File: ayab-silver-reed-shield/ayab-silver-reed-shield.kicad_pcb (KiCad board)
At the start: 2 copper layers, 68.6 x 53.3 mm, 19 parts, among them J1 Power, J2 Digital/PWM, J3 Analog, J4 Digital/PWM, J5 DIN-7, J6 Barrel_Jack, K1 Relay_SPST-NO, Q1 2N2222A-TO92

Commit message: Update PCB design
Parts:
- removed C2: 100u, Locals:CP_6.3x11mm_horiz-R
- added C1: 100u, Locals:CP_6.3x11mm_horiz-R, F.Cu at (125.8, 89.0)
- D1: footprint Diode_THT:D_T-1_P5.08mm_Horizontal -> Diode_THT:D_DO-41_SOD81_P7.62mm_Horizontal
- Q1: footprint PCM_Package_TO_SOT_THT_AKL:TO-92_Inline_Wide_EBC -> Package_TO_SOT_THT:TO-92_Inline
- moved D1 1.76 mm to (115.0, 61.8)
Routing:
- net Net-(D1-A): track 27.2 -> 33.0 mm
- net Net-(C1-Pad1): track 22.3 -> 24.0 mm
- net Net-(Q1-B): track 7.32 -> 7.85 mm

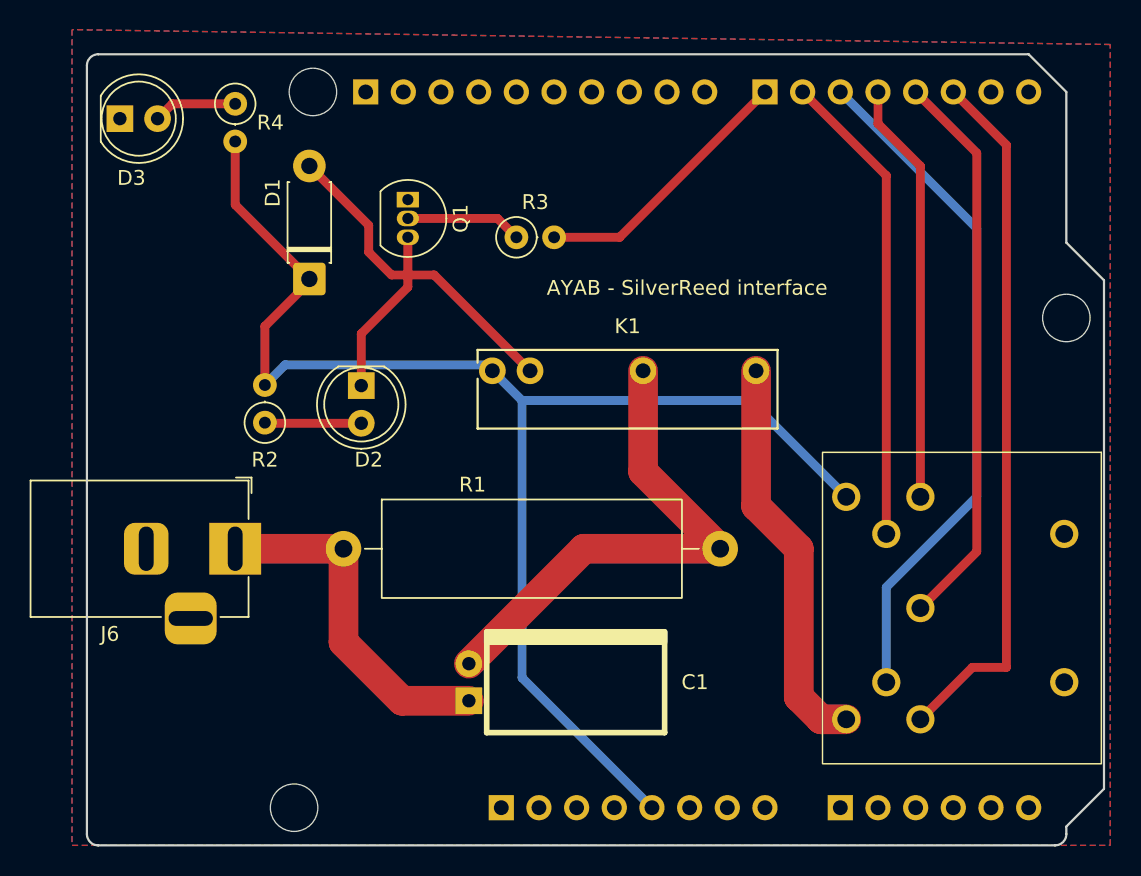
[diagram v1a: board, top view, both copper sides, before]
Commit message: fix: invert din pins
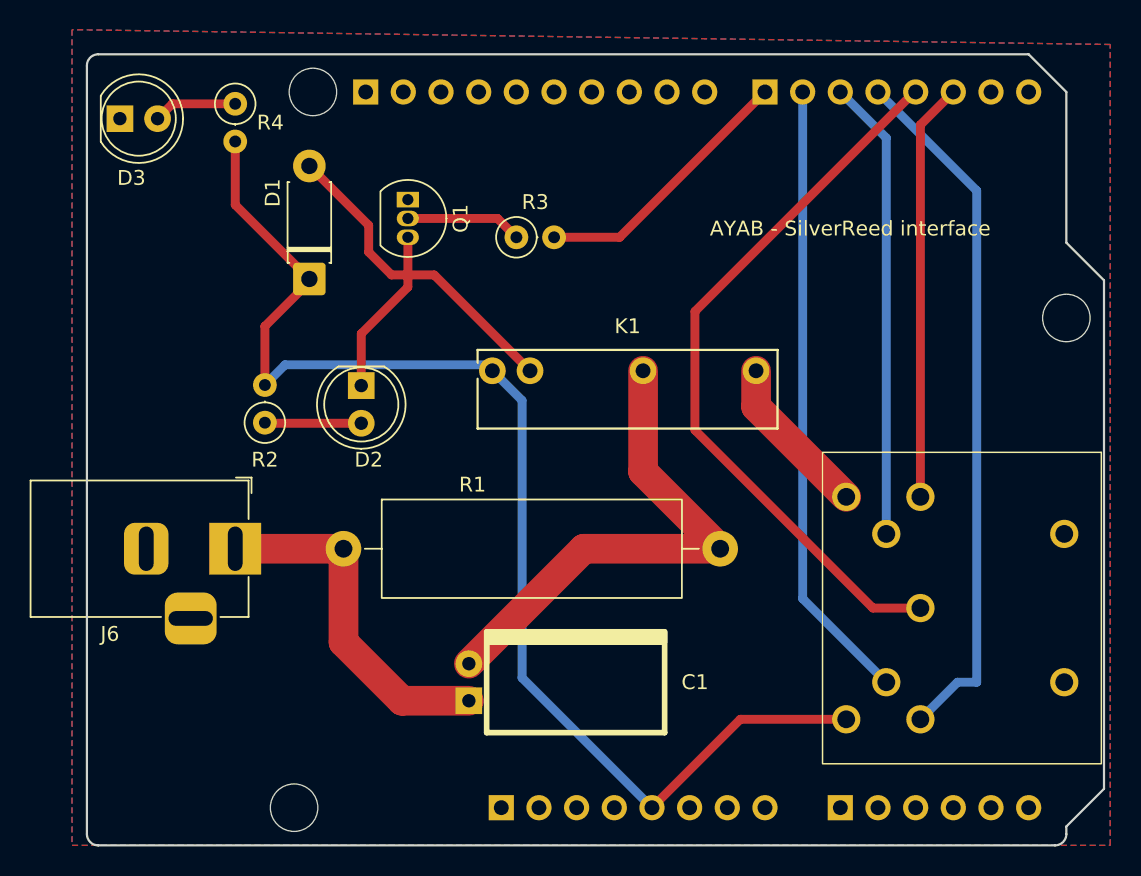
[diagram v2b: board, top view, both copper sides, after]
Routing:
- net /2: track 47.5 -> 28.2 mm
- net /4: track 28.6 -> 47.5 mm
- net Net-(J5-Pad6): track 27.0 -> 11.0 mm
- net /*5: track 46.1 -> 31.1 mm
- net /*3: track 38.1 -> 49.2 mm
- net /*6: track 32.1 -> 42.1 mm
- net +5V: track 94.3 -> 85.3 mm
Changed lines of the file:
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@@
 		(grid_origin 100 100)
 		(pcbplotparams
-			(layerselection 0x00000000_00000000_55555555_5555fff5)
+			(layerselection 0x00000000_00000000_55555555_5755f5ff)
 			(plot_on_all_layers_selection 0x00000000_00000000_00000000_00000000)
 			(disableapertmacros no)
 			(usegerberextensions no)
-			(usegerberattributes yes)
-			(usegerberadvancedattributes yes)
-			(creategerberjobfile yes)
+			(usegerberattributes no)
+			(usegerberadvancedattributes no)
+			(creategerberjobfile no)
 			(dashed_line_dash_ratio 12.000000)
 			(dashed_line_gap_ratio 3.000000)
@@
 			(drillshape 0)
 			(scaleselection 1)
-			(outputdirectory "../../../Downloads/")
+			(outputdirectory "Gerber/")
 		)
 	)
@@
 		)
 		(pad "1" thru_hole circle
-			(at 7.5 2.8 270)
+			(at -7.5 2.8 270)
 			(size 1.905 1.905)
 			(drill 1.2)
@@
 		)
 		(pad "3" thru_hole circle
-			(at -7.5 2.8 270)
+			(at 7.5 2.8 270)
 			(size 1.905 1.905)
 			(drill 1.2)
@@
 		)
 		(pad "4" thru_hole circle
-			(at 5 5.1 270)
+			(at -5 5.1 270)
 			(size 1.905 1.905)
 			(drill 1.2)
@@
 		)
 		(pad "5" thru_hole circle
-			(at -5 5.1 270)
+			(at 5 5.1 270)
 			(size 1.905 1.905)
 			(drill 1.2)
@@
 		)
 		(pad "6" thru_hole circle
-			(at 7.5 7.8 270)
+			(at -7.5 7.8 270)
 			(size 1.905 1.905)
 			(drill 1.2)
@@
 		)
 		(pad "7" thru_hole circle
-			(at -7.5 7.8 270)
+			(at 7.5 7.8 270)
 			(size 1.905 1.905)
 			(drill 1.2)
@@
 			(remove_unused_layers no)
 			(net 1 "GND")
-			(pinfunction "GNG")
+			(pinfunction "GND")
 			(pintype "passive")
 		)
@@
 			(remove_unused_layers no)
 			(net 1 "GND")
-			(pinfunction "GNG")
+			(pinfunction "GND")
 			(pintype "passive")
 		)
@@
 	)
 	(gr_text "AYAB - SilverReed interface\n"
-		(at 131 63 0)
+		(at 142 59 0)
 		(layer "F.SilkS")
 		(effects
@@
 	)
 	(segment
+		(start 138.1 97.46)
+		(end 144.06 91.5)
+		(width 0.6)
+		(layer "F.Cu")
+		(net 3)
+	)
+	(segment
 		(start 110 56.81)
 		(end 115 61.81)
@@
 	)
 	(segment
-		(start 144.7 70)
-		(end 129.34 70)
+		(start 144.06 91.5)
+		(end 151.2 91.5)
 		(width 0.6)
-		(layer "B.Cu")
+		(layer "F.Cu")
 		(net 3)
 	)
@@
 	)
 	(segment
-		(start 151.2 76.5)
-		(end 144.7 70)
-		(width 0.6)
-		(layer "B.Cu")
-		(net 3)
-	)
-	(segment
 		(start 135.92 59)
 		(end 145.72 49.2)
@@
 	(segment
 		(start 153.34 49.2)
-		(end 153.34 51.34)
+		(end 153.2 49.2)
 		(width 0.6)
 		(layer "F.Cu")
@@
 	)
 	(segment
-		(start 153.34 49.2)
-		(end 153.2 49.2)
+		(start 158.7 89)
+		(end 156.2 91.5)
 		(width 0.6)
-		(layer "F.Cu")
+		(layer "B.Cu")
 		(net 19)
 	)
 	(segment
-		(start 153.34 51.34)
-		(end 156.2 54.2)
+		(start 160 89)
+		(end 158.7 89)
 		(width 0.6)
-		(layer "F.Cu")
+		(layer "B.Cu")
 		(net 19)
 	)
 	(segment
-		(start 156.2 54.2)
-		(end 156.2 76.5)
+		(start 160 55.86)
+		(end 160 89)
 		(width 0.6)
-		(layer "F.Cu")
+		(layer "B.Cu")
 		(net 19)
 	)
 	(segment
-		(start 162 52.78)
-		(end 162 88)
+		(start 153.34 49.2)
+		(end 160 55.86)
 		(width 0.6)
-		(layer "F.Cu")
-		(net 20)
+		(layer "B.Cu")
+		(net 19)
 	)
 	(segment
 		(start 158.42 49.2)
-		(end 162 52.78)
-		(width 0.6)
-		(layer "F.Cu")
-		(net 20)
-	)
-	(segment
-		(start 162 88)
-		(end 159.7 88)
+		(end 156.2 51.42)
 		(width 0.6)
 		(layer "F.Cu")
@@
 	)
 	(segment
-		(start 159.7 88)
-		(end 156.2 91.5)
+		(start 156.2 51.42)
+		(end 156.2 76.5)
 		(width 0.6)
 		(layer "F.Cu")
@@
 	)
 	(segment
-		(start 153.9 54.84)
-		(end 153.9 79)
+		(start 148.26 49.2)
+		(end 148.26 83.36)
 		(width 0.6)
-		(layer "F.Cu")
+		(layer "B.Cu")
 		(net 21)
 	)
 	(segment
-		(start 148.26 49.2)
-		(end 153.9 54.84)
+		(start 148.26 83.36)
+		(end 153.9 89)
 		(width 0.6)
-		(layer "F.Cu")
+		(layer "B.Cu")
 		(net 21)
 	)
 	(segment
-		(start 160 58.4)
-		(end 160 76.5)
+		(start 150.8 49.2)
+		(end 153.9 52.3)
 		(width 0.6)
 		(layer "B.Cu")
@@
 	)
 	(segment
-		(start 153.9 82.6)
-		(end 153.9 89)
+		(start 153.9 52.3)
+		(end 153.9 79)
 		(width 0.6)
 		(layer "B.Cu")
@@
 	)
 	(segment
-		(start 150.8 49.2)
-		(end 160 58.4)
+		(start 141 72)
+		(end 153 84)
 		(width 0.6)
-		(layer "B.Cu")
-		(net 22)
+		(layer "F.Cu")
+		(net 24)
 	)
 	(segment
-		(start 160 76.5)
-		(end 153.9 82.6)
+		(start 141 64)
+		(end 141 72)
 		(width 0.6)
-		(layer "B.Cu")
-		(net 22)
+		(layer "F.Cu")
+		(net 24)
 	)
 	(segment
-		(start 155.88 49.2)
-		(end 160 53.32)
+		(start 155.8 49.2)
+		(end 141 64)
 		(width 0.6)
 		(layer "F.Cu")
@@
 	)
 	(segment
-		(start 160 80.2)
-		(end 156.2 84)
+		(start 155.88 49.2)
+		(end 155.8 49.2)
 		(width 0.6)
 		(layer "F.Cu")
@@
 	)
 	(segment
-		(start 160 53.32)
-		(end 160 80.2)
+		(start 153 84)
+		(end 156.2 84)
 		(width 0.6)
 		(layer "F.Cu")
@@
 	)
 	(segment
-		(start 145.12 68)
-		(end 145.12 77.12)
-		(width 2)
-		(layer "F.Cu")
-		(net 34)
-	)
-	(segment
-		(start 148 90)
-		(end 149.5 91.5)
-		(width 2)
-		(layer "F.Cu")
-		(net 34)
-	)
-	(segment
-		(start 149.5 91.5)
-		(end 151.2 91.5)
+		(start 145.12 70.42)
+		(end 151.2 76.5)
 		(width 2)
 		(layer "F.Cu")
@@
 	)
 	(segment
-		(start 145.12 77.12)
-		(end 148 80)
-		(width 2)
-		(layer "F.Cu")
-		(net 34)
-	)
-	(segment
-		(start 148 80)
-		(end 148 90)
+		(start 145.12 68)
+		(end 145.12 70.42)
 		(width 2)
 		(layer "F.Cu")

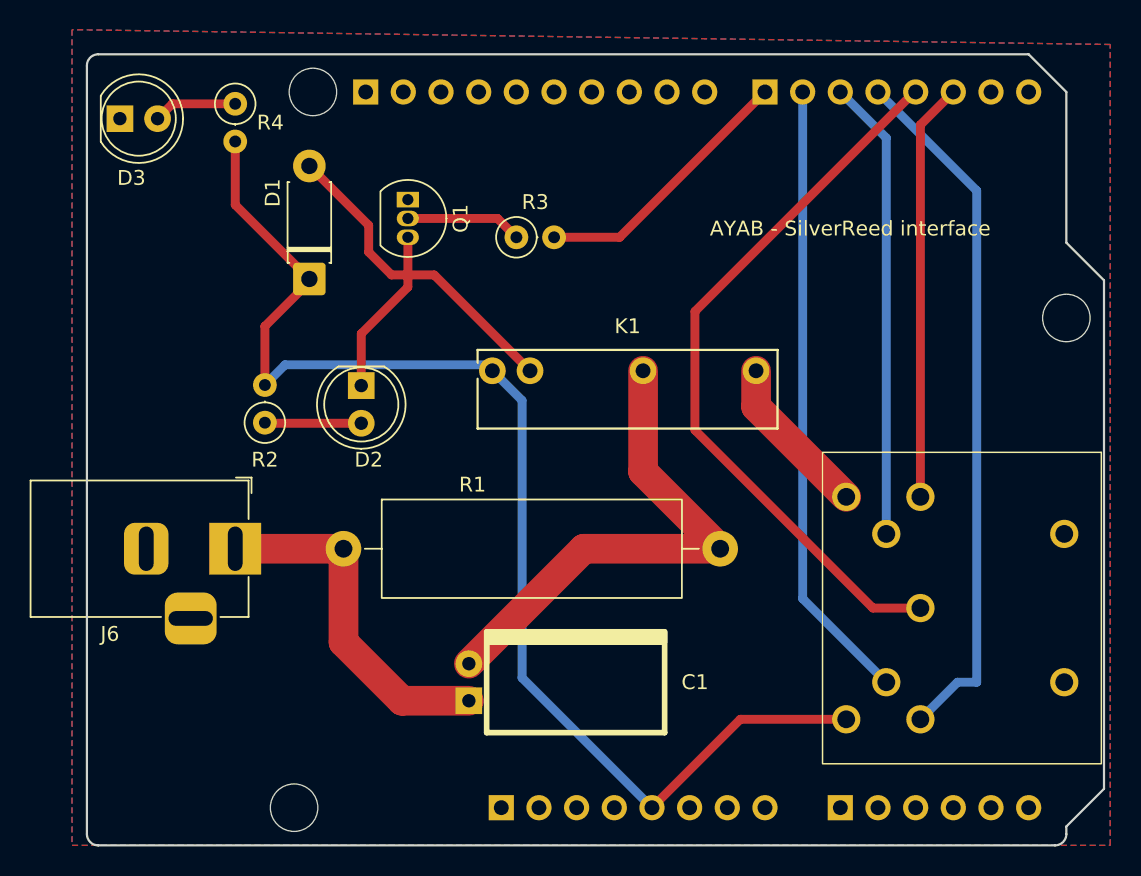
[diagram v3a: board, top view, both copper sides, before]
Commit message: feat: new board version with debug
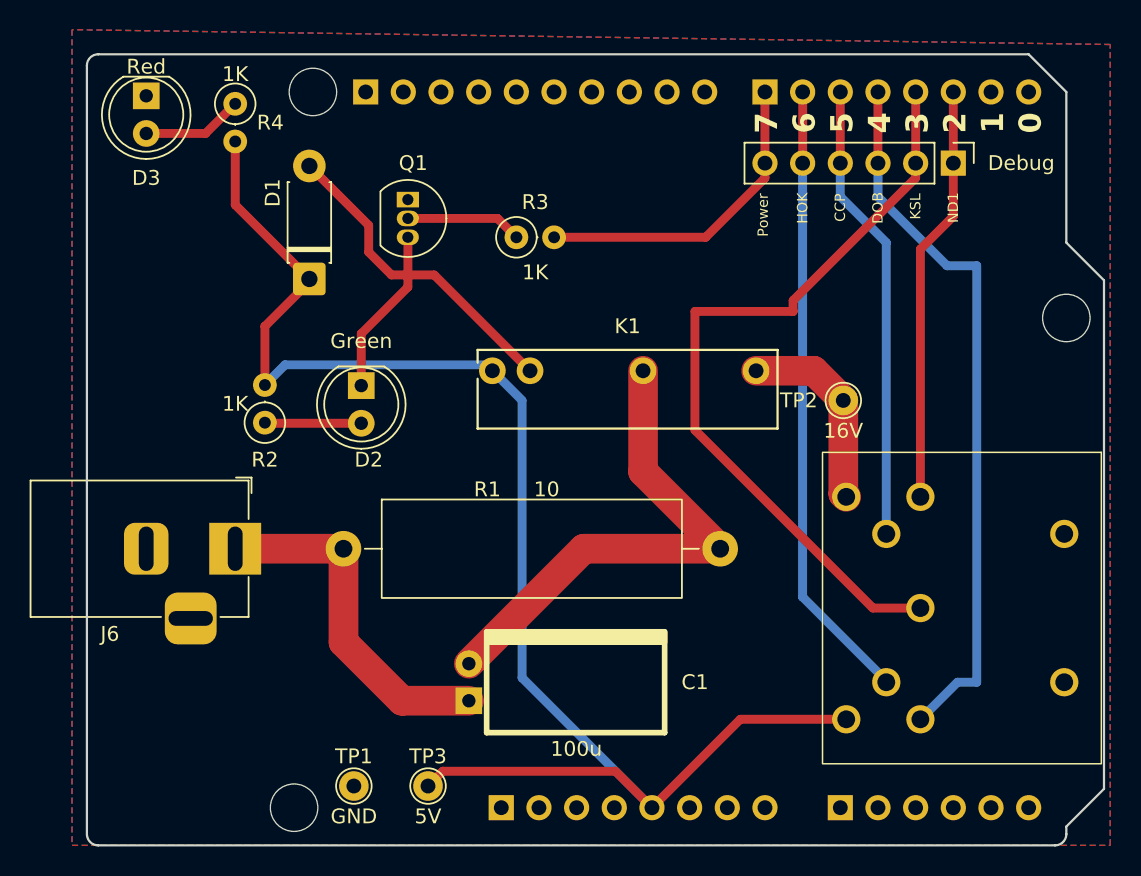
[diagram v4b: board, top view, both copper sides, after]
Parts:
- added J7: Debug, Connector_PinHeader_2.54mm:PinHeader_1x06_P2.54mm_Vertical, F.Cu at (158.4, 54.0)
- added TP1: GND, TestPoint:TestPoint_THTPad_D2.0mm_Drill1.0mm, F.Cu at (118.0, 96.0)
- added TP2: 16V, TestPoint:TestPoint_THTPad_D2.0mm_Drill1.0mm, F.Cu at (151.0, 70.0)
- added TP3: 5V, TestPoint:TestPoint_THTPad_D2.0mm_Drill1.0mm, F.Cu at (123.0, 96.0)
- moved D3 2.35 mm to (104.0, 49.5), turned to -90 degrees
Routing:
- net +5V: track 85.3 -> 101.8 mm
- net /7: track 18.3 -> 22.6 mm
- net /*3: track 49.2 -> 53.1 mm
- net Net-(J5-Pad6): track 11.0 -> 13.3 mm
- net Net-(D3-A): track 5.65 -> 6.83 mm
- net /4: track 47.5 -> 48.7 mm
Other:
- board text added: "0"
- board text added: "1"
- board text added: "2"
- board text added: "3"
- board text added: "4"
- board text added: "5"
- board text added: "6"
- board text added: "7"
- board text added: "CCP"
- board text added: "DOB"
- board text added: "HOK"
- board text added: "KSL"
- board text added: "ND1"
- board text added: "Power"
- board text removed: "AYAB - SilverReed interface"

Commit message: wip
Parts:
- J7: value Debug -> DebugPorts
- TP1, TP2, TP3: footprint TestPoint:TestPoint_THTPad_D2.0mm_Drill1.0mm -> TestPoint:TestPoint_Pad_D1.0mm
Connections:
- net /*3 renamed KSL
- net /*5 renamed CCP
- net /*6 renamed HOK
- net /2 renamed ND1
- net /4 renamed DOB
- net /7 renamed SOLENOID_CONTROL
